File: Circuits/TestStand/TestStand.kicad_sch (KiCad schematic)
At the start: 87 parts, among them IC1 STP85NF55, J1 Screw_Terminal_01x07, J10 Screw_Terminal_01x03, J11 Screw_Terminal_01x03, J12 Screw_Terminal_01x03, J13 Screw_Terminal_01x03, J14 Screw_Terminal_01x02, J15 Conn_Coaxial, J16 Screw_Terminal_01x02, J2 Screw_Terminal_01x07, J3 Screw_Terminal_01x07, J4 Screw_Terminal_01x03, J5 Screw_Terminal_01x03, J6 Screw_Terminal_01x03, J7 Screw_Terminal_01x03, J8 Screw_Terminal_01x03, J9 Screw_Terminal_01x03, Q1 MMBT4403-7-F, Q2 MMBT4403-7-F, Q3 MMBT4403-7-F, U1 HX711, U2 HX711, U3 HX711, U4 Teensy4.1, U5 LP2980IM5X-3.3/NOPB, U6 MAX31855KASA, U7 NRF24L01, U8 LP2980IM5X-3.3/NOPB, Y1 16Mhz

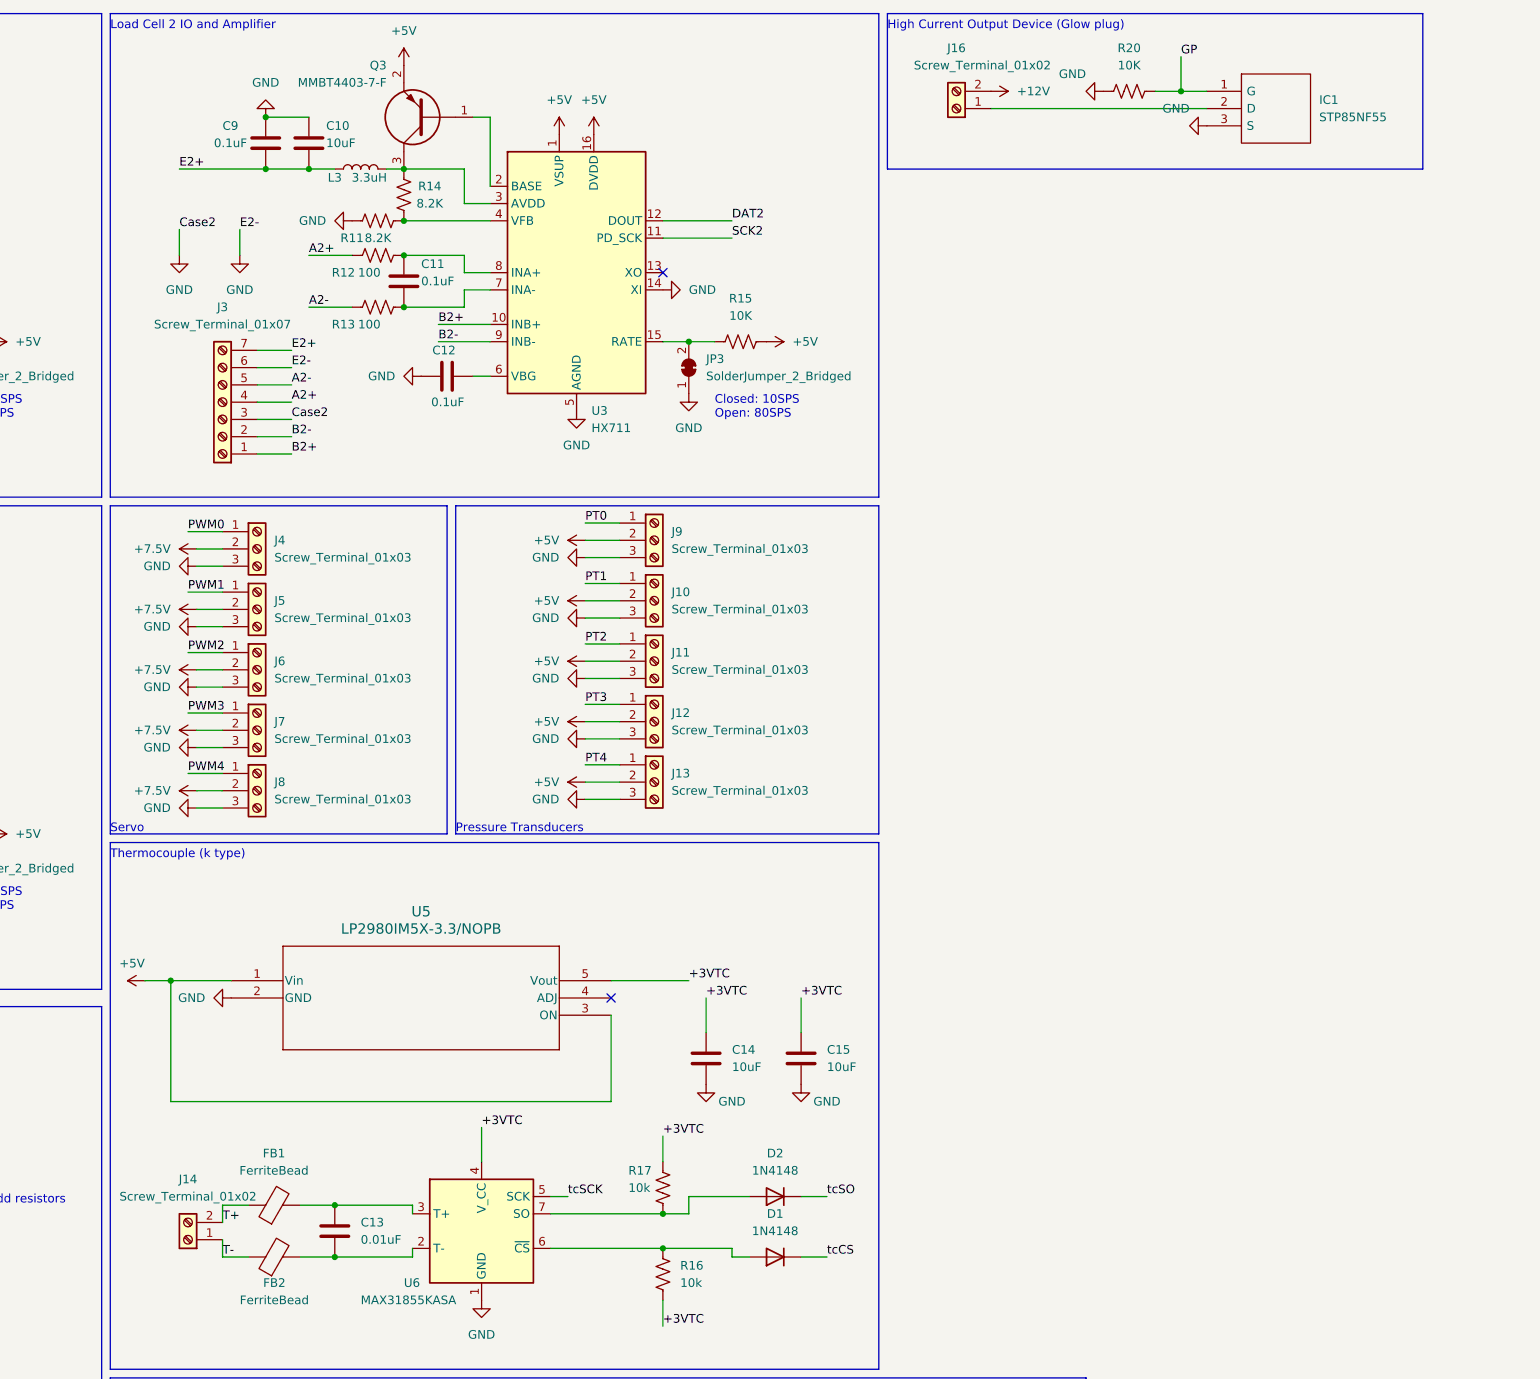
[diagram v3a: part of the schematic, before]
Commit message: added voltage regulator stuff
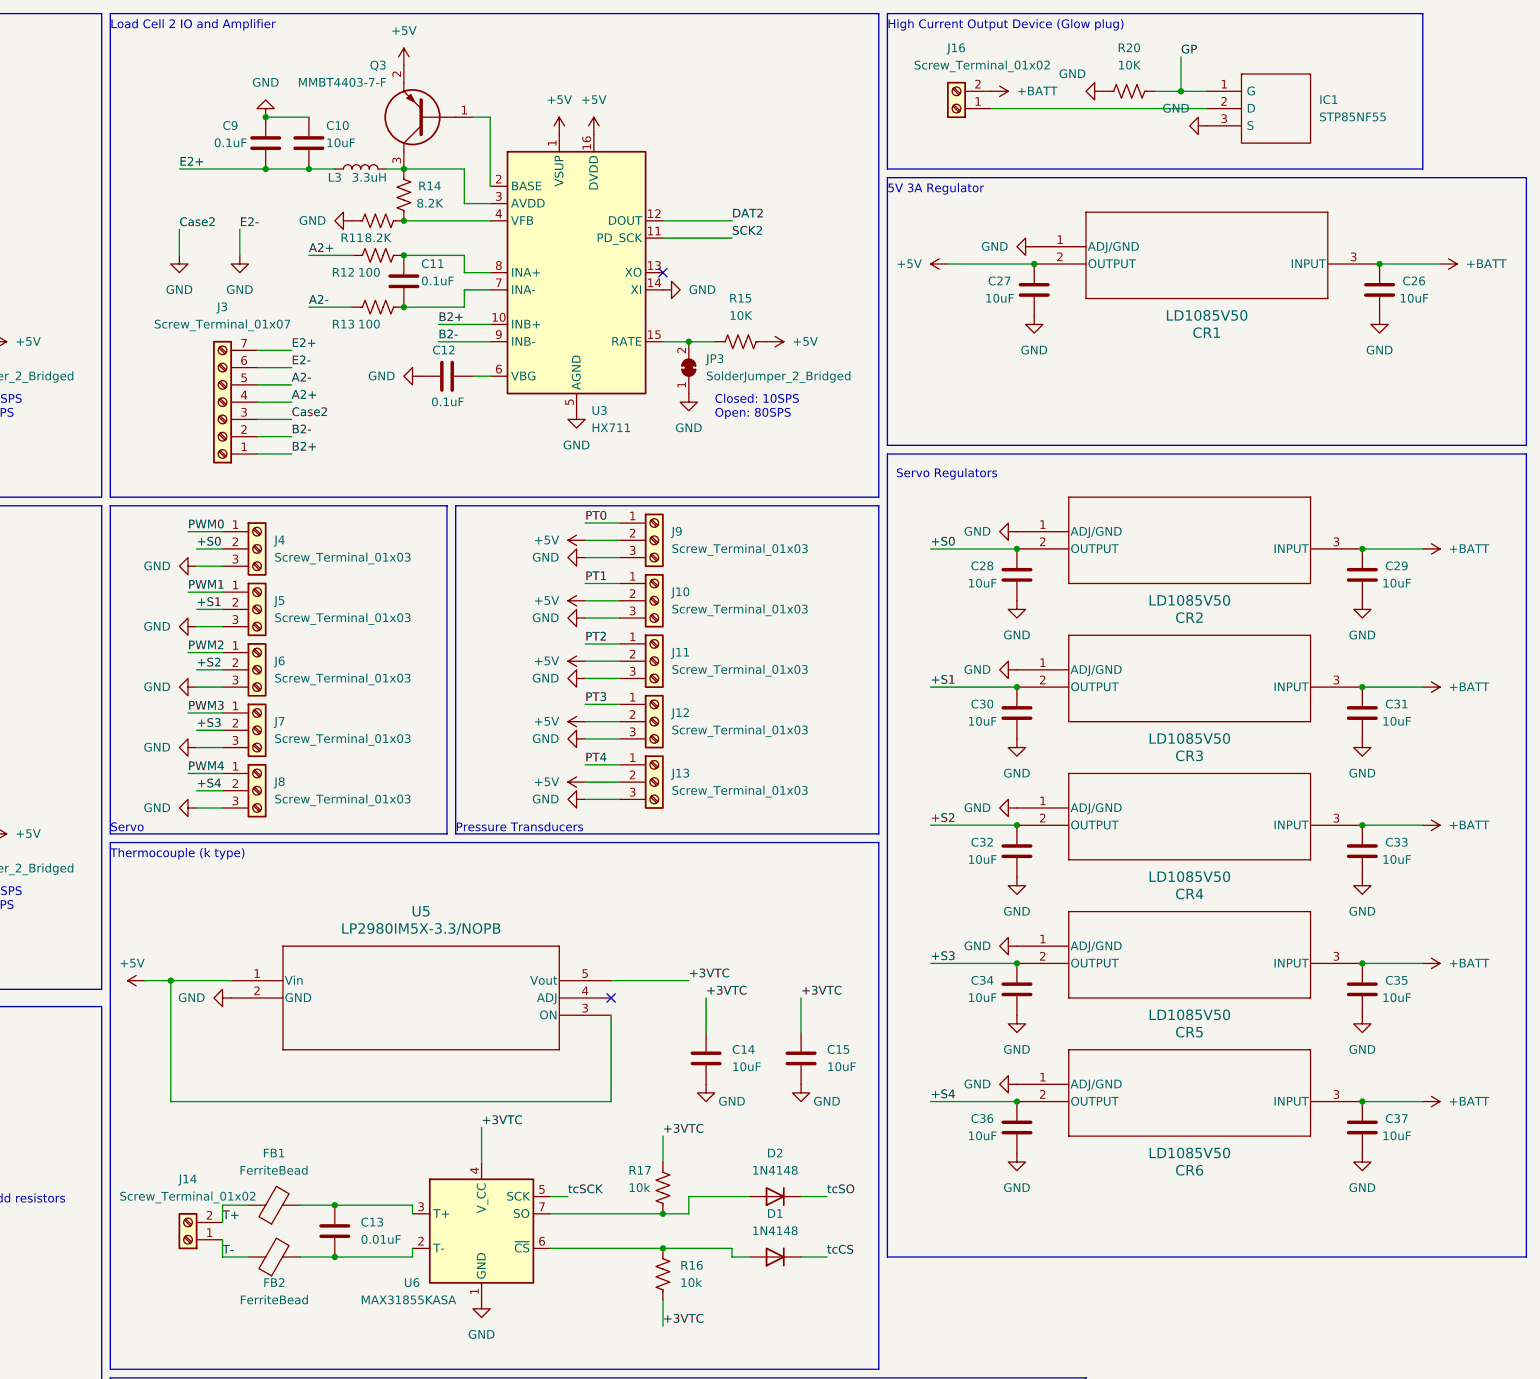
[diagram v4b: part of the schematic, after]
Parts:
- added C26, C27, C28, C29, C30, C31, C32, C33, C34, C35, C36, C37: 10uF, Capacitor_SMD:C_0805_2012Metric, symbol Device:C
- added CR1, CR2, CR3, CR4, CR5, CR6: LD1085V50, Library:TO-220_STM, symbol 2024-08-13_22-25-40:LD1085V50
- IC1: footprint TO255P460X1020X2008-3P -> Library:TO255P460X1020X2008-3P
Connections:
- net +5V: now also C27.2, CR1.2 (OUTPUT)
- net GND: now also C26.1, C27.1, C28.1, C29.1, C30.1, C31.1, C32.1, C33.1, C34.1, C35.1, C36.1, C37.1, CR1.1 (ADJ/GND), CR2.1 (ADJ/GND), CR3.1 (ADJ/GND), CR4.1 (ADJ/GND), CR5.1 (ADJ/GND), CR6.1 (ADJ/GND)
- net +12V renamed +BATT
- net +BATT: now also C26.2, C29.2, C31.2, C33.2, C35.2, C37.2, CR1.3 (INPUT), CR2.3 (INPUT), CR3.3 (INPUT), CR4.3 (INPUT), CR5.3 (INPUT), CR6.3 (INPUT)
- removed net +7.5V: J4.2 (Pin_2), J5.2 (Pin_2), J6.2 (Pin_2), J7.2 (Pin_2), J8.2 (Pin_2)
- new net +S0: C28.2, CR2.2 (OUTPUT), J4.2 (Pin_2)
- new net +S1: C30.2, CR3.2 (OUTPUT), J5.2 (Pin_2)
- new net +S2: C32.2, CR4.2 (OUTPUT), J6.2 (Pin_2)
- new net +S3: C34.2, CR5.2 (OUTPUT), J7.2 (Pin_2)
- new net +S4: C36.2, CR6.2 (OUTPUT), J8.2 (Pin_2)
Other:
- note added: "5V 3A Regulator"
- note added: "Servo Regulators"

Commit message: Lots of tracing, filleting board shape
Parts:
- added H1, H2, H3, H4: MountingHole_Pad, MountingHole:MountingHole_3.2mm_M3_Pad, symbol Mechanical:MountingHole_Pad
- added J17: Screw_Terminal_01x02, Connector_Wago:Wago_734-132_1x02_P3.50mm_Vertical, symbol Connector:Screw_Terminal_01x02
- added SW1: SW_DIP_x01, Button_Switch_THT:SW_DIP_SPSTx01_Slide_6.7x4.1mm_W7.62mm_P2.54mm_LowProfile, symbol Switch:SW_DIP_x01
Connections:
- net +BATT: now also J17.2 (Pin_2)
- net GND: now also H1.1, H2.1, H3.1, H4.1, SW1.2
- new net: J17.1 (Pin_1), SW1.1
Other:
- note added: "Battery Terminal and Switch"

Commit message: Very important silkscreen additions
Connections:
- no-connect marks 5 -> 42
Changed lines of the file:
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@@
   (junction (at 173.99 48.26) (diameter 0) (color 0 0 0 0)
   )
+  (no_connect (at 96.52 248.92))
+  (no_connect (at 40.64 242.57))
+  (no_connect (at 40.64 212.09))
   (no_connect (at 97.79 55.88))
+  (no_connect (at 40.64 248.92))
+  (no_connect (at 40.64 251.46))
+  (no_connect (at 96.52 224.79))
+  (no_connect (at 96.52 189.23))
+  (no_connect (at 40.64 217.17))
+  (no_connect (at 40.64 254))
+  (no_connect (at 40.64 234.95))
+  (no_connect (at 72.39 264.16))
+  (no_connect (at 40.64 229.87))
+  (no_connect (at 64.77 264.16))
+  (no_connect (at 96.52 214.63))
+  (no_connect (at 76.2 264.16))
+  (no_connect (at 96.52 181.61))
+  (no_connect (at 96.52 194.31))
+  (no_connect (at 40.64 246.38))
+  (no_connect (at 96.52 209.55))
+  (no_connect (at 96.52 251.46))
   (no_connect (at 212.09 55.88))
+  (no_connect (at 96.52 243.84))
+  (no_connect (at 68.58 264.16))
+  (no_connect (at 40.64 214.63))
   (no_connect (at 204.47 162.56))
+  (no_connect (at 96.52 227.33))
   (no_connect (at 209.55 285.75))
+  (no_connect (at 96.52 184.15))
+  (no_connect (at 40.64 232.41))
+  (no_connect (at 96.52 172.72))
+  (no_connect (at 96.52 254))
+  (no_connect (at 96.52 246.38))
+  (no_connect (at 96.52 241.3))
+  (no_connect (at 40.64 209.55))
   (no_connect (at 97.79 128.27))
+  (no_connect (at 60.96 264.16))
+  (no_connect (at 40.64 256.54))
+  (no_connect (at 96.52 186.69))
+  (no_connect (at 96.52 191.77))
+  (no_connect (at 40.64 240.03))
+  (no_connect (at 96.52 217.17))
   (wire (pts (xy 144.78 300.99) (xy 144.78 283.21))
     (stroke (width 0) (type default))

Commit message: Schematic cleanup
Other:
- note added: "M3 Holes"
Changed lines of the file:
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@@
+    (fill (type none))
+  )
+  (rectangle (start 340.36 52.07) (end 370.84 77.47)
+    (stroke (width 0) (type default))
     (fill (type none))
   )
@@
     (effects (font (size 1.27 1.27)) (justify left bottom))
   )
+  (text "M3 Holes" (at 341.63 76.2 0)
+    (effects (font (size 1.27 1.27)) (justify left bottom))
+  )

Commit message: assigned a bunch of components to real ones
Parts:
- removed SW1: SW_DIP_x01, Button_Switch_THT:SW_DIP_SPSTx01_Slide_6.7x4.1mm_W7.62mm_P2.54mm_LowProfile, symbol Switch:SW_DIP_x01
- C1, C11, C12, C2, C4, C5, C7, C8, C9: LCSC (none) -> C126469
- C10, C14, C15, C23, C26, C27, C28, C29, C3, C30, C31, C32, C33, C34, C35, C36, C37, C6: LCSC (none) -> C15850
- C13, C24: LCSC (none) -> C1710
- C16: LCSC (none) -> C1739
- C17, C18: LCSC (none) -> C1804
- C19: LCSC (none) -> C377773
- C20: LCSC (none) -> C519993
- C21: LCSC (none) -> C1788
- C22: LCSC (none) -> C1786
- C25: LCSC (none) -> C46653
- CR1, CR2, CR3, CR4, CR5, CR6: LCSC (none) -> C283283
- IC1: LCSC (none) -> C3290239
- L1, L2, L3: footprint Inductor_SMD:L_0805_2012Metric -> Inductor_SMD:L_0402_1005Metric; LCSC (none) -> C84474
- L4: footprint Inductor_SMD:L_0805_2012Metric -> Inductor_SMD:L_0402_1005Metric; LCSC (none) -> C77108
- L5: footprint Inductor_SMD:L_0805_2012Metric -> Inductor_SMD:L_0402_1005Metric; LCSC (none) -> C76778
- L6: footprint Inductor_SMD:L_0805_2012Metric -> Inductor_SMD:L_0402_1005Metric; LCSC (none) -> C14033
- Q1, Q2, Q3: LCSC (none) -> C85183
- R1, R10, R15, R16, R17, R20: LCSC (none) -> C17414
- R11, R14, R4, R5, R6, R9: LCSC (none) -> C17828
- R12, R13, R2, R3, R7, R8: LCSC (none) -> C17408
- R18: LCSC (none) -> C17560
- R19: LCSC (none) -> C17514
- U1, U2, U3: LCSC (none) -> C6705483
- U5, U8: LCSC (none) -> C88715
- U6: LCSC (none) -> C52028
- U7: LCSC (none) -> C8791
- Y1: footprint Crystal:Crystal_SMD_2012-2Pin_2.0x1.2mm -> Crystal:Crystal_SMD_5032-2Pin_5.0x3.2mm; LCSC (none) -> C122519
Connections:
- net GND: now also J17.1 (Pin_1)
